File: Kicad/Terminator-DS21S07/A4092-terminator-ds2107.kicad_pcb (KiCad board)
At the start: 2 copper layers, 72.3 x 17.6 mm, 10 parts, among them J1 Conn_02x25_Odd_Even, U1 LT1118-2.85

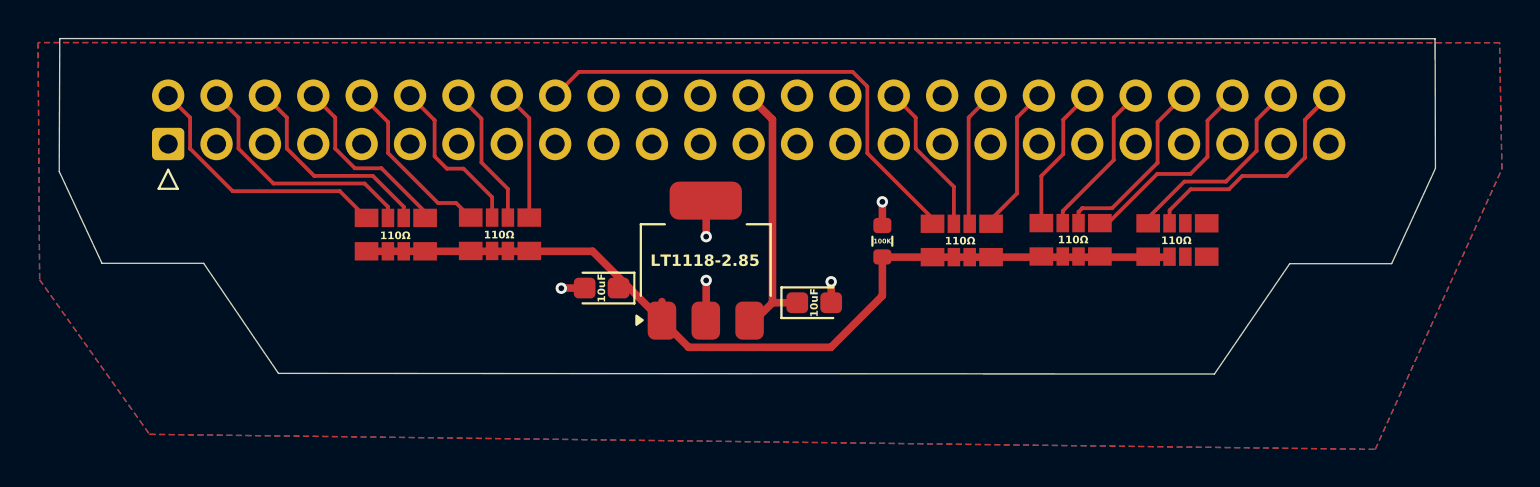
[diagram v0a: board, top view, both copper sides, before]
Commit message: Finish DS2107 terminator
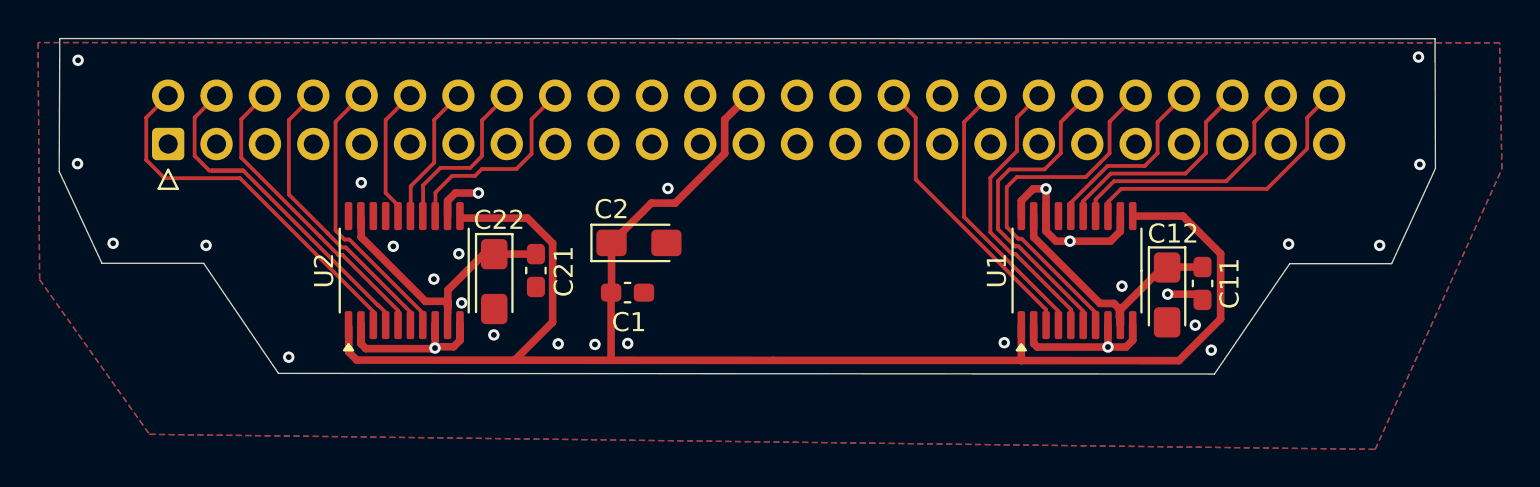
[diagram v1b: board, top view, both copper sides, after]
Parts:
- removed R3: 100K, Resistor_SMD:R_0603_1608Metric
- removed RN1, RN2, RN3, RN4, RN5: 110Ω, CAY16_102J4LF:BO_CAY16
- added C11: 100nF, Capacitor_SMD:C_0603_1608Metric_Pad1.08x0.95mm_HandSolder, F.Cu at (146.0, 46.3)
- added C12: 4.7uF, Capacitor_Tantalum_SMD:CP_EIA-3216-10_Kemet-I_HandSolder, F.Cu at (144.2, 46.9)
- added C21: 100nF, Capacitor_SMD:C_0603_1608Metric_Pad1.08x0.95mm_HandSolder, F.Cu at (111.0, 45.6)
- added C22: 4.7uF, Capacitor_Tantalum_SMD:CP_EIA-3216-10_Kemet-I_HandSolder, F.Cu at (108.8, 46.2)
- added U2: DS21S07A, Package_SO:TSSOP-20_4.4x6.5mm_P0.65mm, F.Cu at (104.1, 45.6)
- C1: value 10uF -> 100nF; footprint Capacitor_Tantalum_SMD:CP_EIA-2012-12_Kemet-R -> Capacitor_SMD:C_0603_1608Metric_Pad1.08x0.95mm_HandSolder
- C2: value 10uF -> 4.7uF; footprint Capacitor_Tantalum_SMD:CP_EIA-2012-12_Kemet-R -> Capacitor_Tantalum_SMD:CP_EIA-3216-10_Kemet-I_HandSolder
- U1: value LT1118-2.85 -> DS21S07A; footprint Package_TO_SOT_SMD:SOT-223-3_TabPin2 -> Package_SO:TSSOP-20_4.4x6.5mm_P0.65mm
- moved U1 19.5 mm to (139.4, 45.6)
- moved C1 9.82 mm to (115.8, 46.8)
- moved C2 3.08 mm to (116.5, 44.2), turned to 0 degrees
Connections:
- C2 pad 1: 2V85 -> SCSI_TERMPWR
- J1 pad 34: unconnected-(J1-Pin_34-Pad34) -> GND
- U1 pad 1: 2V85 -> SCSI_TERMPWR
- U1 pad 3: SCSI_TERMPWR -> SCTRL_ATN
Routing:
- net SCSI_TERMPWR: track 14.6 -> 88.9 mm
- net 2V85: track 49.0 -> 0.00 mm
- net GND: track 7.73 -> 33.6 mm, vias 5 -> 29
- net SCDATP: track 25.8 -> 10.8 mm
- net VREF1: track 0.00 -> 13.8 mm
- net VREF2: track 0.00 -> 13.7 mm
- net SCTRL_RST: track 7.69 -> 18.8 mm
- net SCTRL_MSG: track 8.28 -> 19.0 mm
- net SCTRL_BSY: track 7.23 -> 14.7 mm
- net SCTRL_ATN: track 8.03 -> 15.4 mm
- net SCDAT1: track 13.0 -> 20.0 mm
- net SCTRL_ACK: track 7.77 -> 14.3 mm
- net SCDAT0: track 14.0 -> 19.9 mm
- net SCDAT3: track 9.67 -> 15.5 mm
- net SCDAT2: track 11.2 -> 16.2 mm
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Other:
- board text removed: "110Ω"
